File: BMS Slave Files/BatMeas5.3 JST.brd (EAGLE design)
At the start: 70 x 35 mm, 49 parts, among them IC1 ATTINY24, IC2 3V3, IC3 3V, J4 BM05B-PASS-1-TFT_(LF)(SN)SMD, T1 MMUN2233, T2 MMUN2233, T3 MMUN2233, T4 MMUN2111LT1G, T5 MMUN2111LT1G, T6 MMUN2111LT1G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

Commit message: Added manufacturing files
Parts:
- C6: value 100n -> 1µ
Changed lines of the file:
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@@
 <attribute name="VALUE" x="37.855" y="23.29" size="0.8128" layer="27" font="vector"/>
 </element>
-<element name="C6" library="rcl" package="C0603" value="100n" x="47.5075" y="14.705" smashed="yes" rot="R90">
+<element name="C6" library="rcl" package="C0603" value="1µ" x="47.5075" y="14.705" smashed="yes" rot="R90">
 <attribute name="NAME" x="48.3925" y="12.91" size="1.016" layer="25" rot="R180"/>
 <attribute name="VALUE" x="49.4125" y="14.07" size="1.27" layer="27" rot="R90"/>

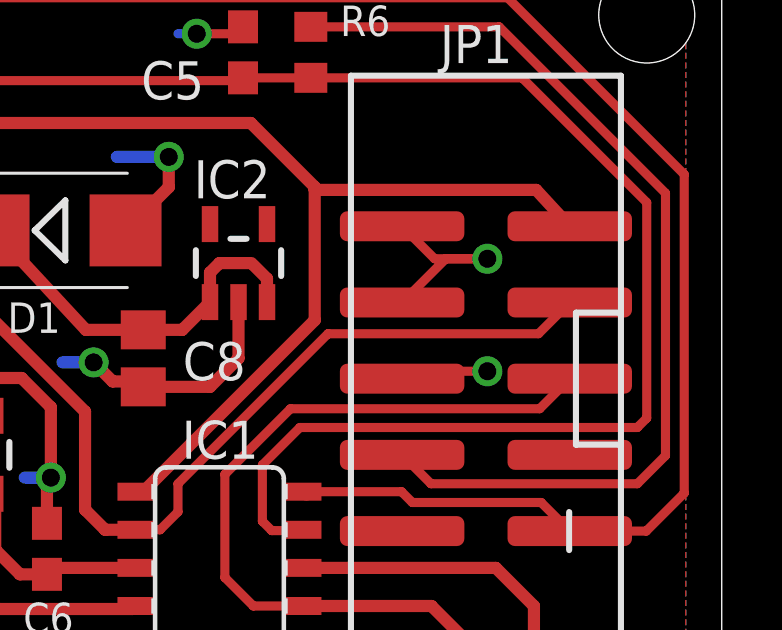
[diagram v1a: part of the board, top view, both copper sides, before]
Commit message: Move vias further away from opposite pin
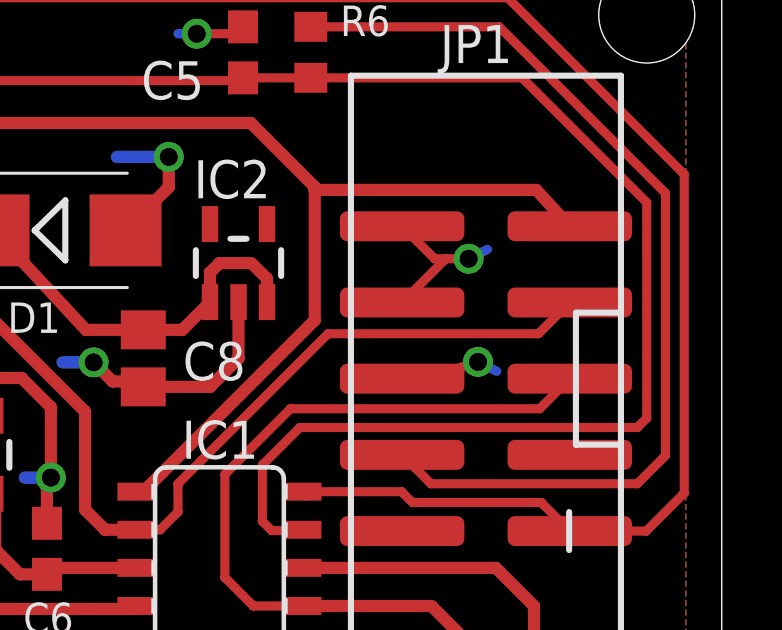
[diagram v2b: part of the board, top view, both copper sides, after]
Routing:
- net GND: track 102.9 -> 101.4 mm
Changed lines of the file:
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@@
 <wire x1="23.125" y1="23.75" x2="24.0625" y2="23.4375" width="0.4064" layer="16"/>
 <wire x1="59.346" y1="22.9175" x2="60.8035" y2="24.375" width="0.3048" layer="1"/>
-<wire x1="60.8035" y1="24.375" x2="62.1875" y2="24.375" width="0.3048" layer="1"/>
-<via x="62.1875" y="24.375" extent="1-16" drill="0.6" shape="octagon"/>
-<wire x1="62.1875" y1="24.375" x2="62.1875" y2="24.6875" width="0.3048" layer="16"/>
+<via x="61.5625" y="24.375" extent="1-16" drill="0.6" shape="octagon"/>
+<wire x1="61.5625" y1="24.375" x2="62.1875" y2="24.6875" width="0.3048" layer="16"/>
 <wire x1="59.346" y1="25.4575" x2="60.4285" y2="24.375" width="0.3048" layer="1"/>
-<wire x1="60.4285" y1="24.375" x2="62.1875" y2="24.375" width="0.3048" layer="1"/>
-<wire x1="59.346" y1="20.3775" x2="59.906" y2="20.625" width="0.3048" layer="1"/>
-<wire x1="59.906" y1="20.625" x2="62.1875" y2="20.625" width="0.3048" layer="1"/>
-<via x="62.1875" y="20.625" extent="1-16" drill="0.6" shape="octagon"/>
-<wire x1="62.1875" y1="20.625" x2="62.5" y2="20.625" width="0.3048" layer="16"/>
+<wire x1="60.4285" y1="24.375" x2="60.8035" y2="24.375" width="0.3048" layer="1"/>
+<wire x1="60.8035" y1="24.375" x2="61.5625" y2="24.375" width="0.3048" layer="1"/>
+<wire x1="59.346" y1="20.3775" x2="59.906" y2="20.3125" width="0.3048" layer="1"/>
+<wire x1="59.906" y1="20.3125" x2="61.875" y2="20.9375" width="0.3048" layer="1"/>
+<via x="61.875" y="20.9375" extent="1-16" drill="0.6" shape="octagon"/>
+<wire x1="61.875" y1="20.9375" x2="62.5" y2="20.625" width="0.3048" layer="16"/>
 <wire x1="54.0425" y1="32.105" x2="53.96" y2="31.875" width="0.3048" layer="1"/>
 <wire x1="53.96" y1="31.875" x2="52.5" y2="31.875" width="0.3048" layer="1"/>
